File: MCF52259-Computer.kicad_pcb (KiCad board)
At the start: 6 copper layers, 110.5 x 130 mm, 4 parts, among them Y1 8MHz

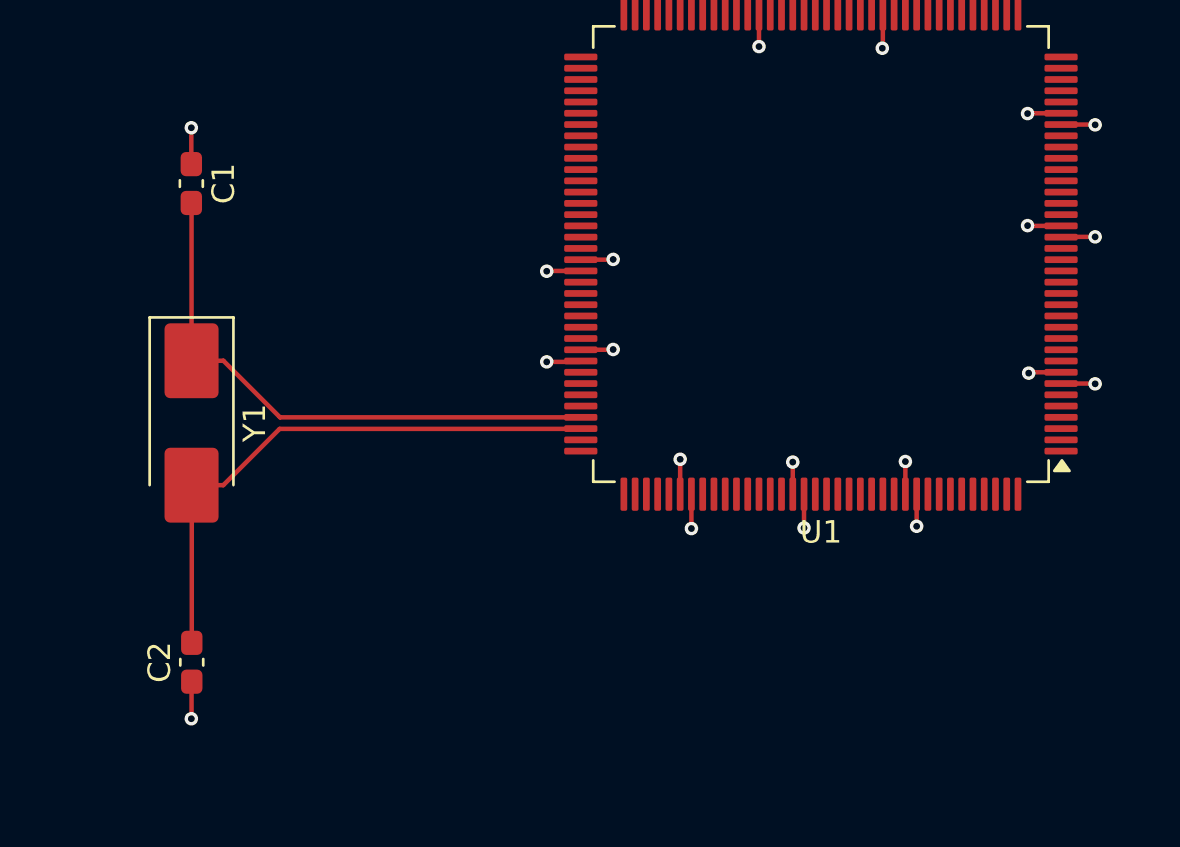
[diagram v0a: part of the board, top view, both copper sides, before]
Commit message: Configured Clock Modes Correctly
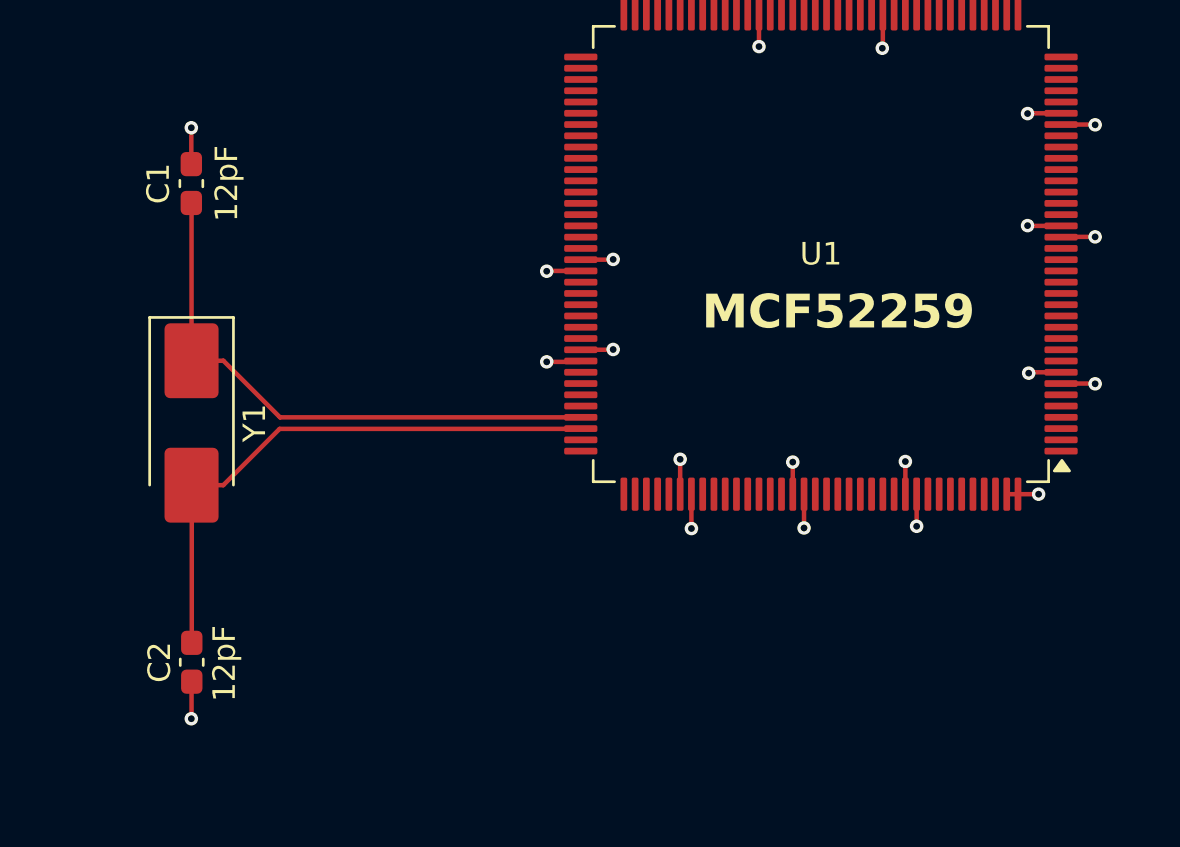
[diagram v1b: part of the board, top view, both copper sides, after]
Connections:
- C1 pad 1: GND -> VSS
- C2 pad 1: GND -> VSS
- U1 pad 113: FEC_TXD2 -> FEC_TXD0
- U1 pad 133: FB_A17 -> FB_A16
- U1 pad 143: CLKMOD0 -> VDD
- U1 pad 144: CLKMOD1 -> VDD
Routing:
- net GND: track 3.24 -> 0.00 mm, vias 2 -> 0
- net VSS: track 14.7 -> 18.0 mm, vias 10 -> 12
- net VDD: track 15.3 -> 16.7 mm, vias 10 -> 11
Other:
- board text added: "MCF52259"

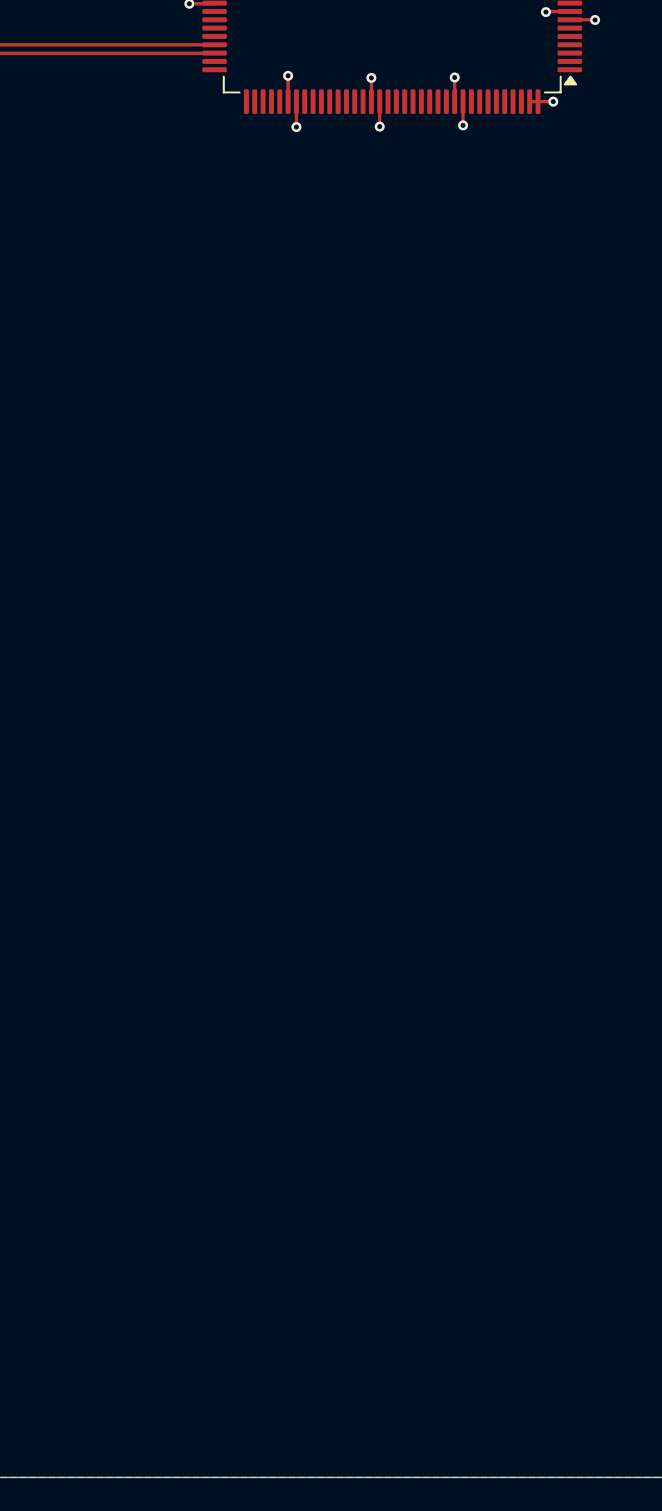
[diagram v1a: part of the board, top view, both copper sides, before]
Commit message: Added Reset Circuitry
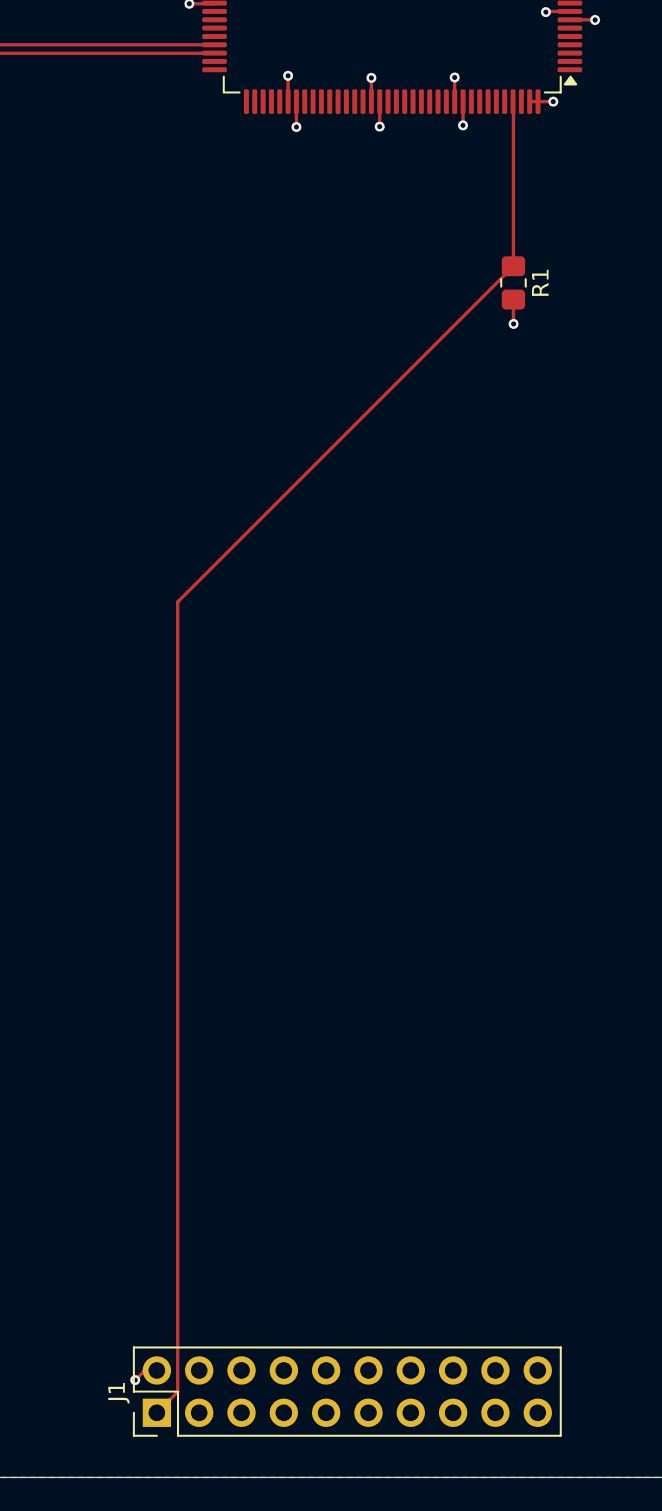
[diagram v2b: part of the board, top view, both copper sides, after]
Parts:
- added J1: Conn_02x10_Counter_Clockwise, Connector_PinHeader_2.54mm:PinHeader_2x10_P2.54mm_Vertical, F.Cu at (89.5, 157.6)
- added R1: 330Ω, Resistor_SMD:R_0805_2012Metric_Pad1.20x1.40mm_HandSolder, F.Cu at (110.8, 89.8)
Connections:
- U1 pad 142: /RSTOUT -> unconnected-(U1-/RSTOUT-Pad142)
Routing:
- net /RSTIN: track 0.00 -> 87.6 mm
- net VSS: track 18.0 -> 19.5 mm, vias 12 -> 13
- net VDD: track 16.7 -> 18.2 mm, vias 11 -> 12

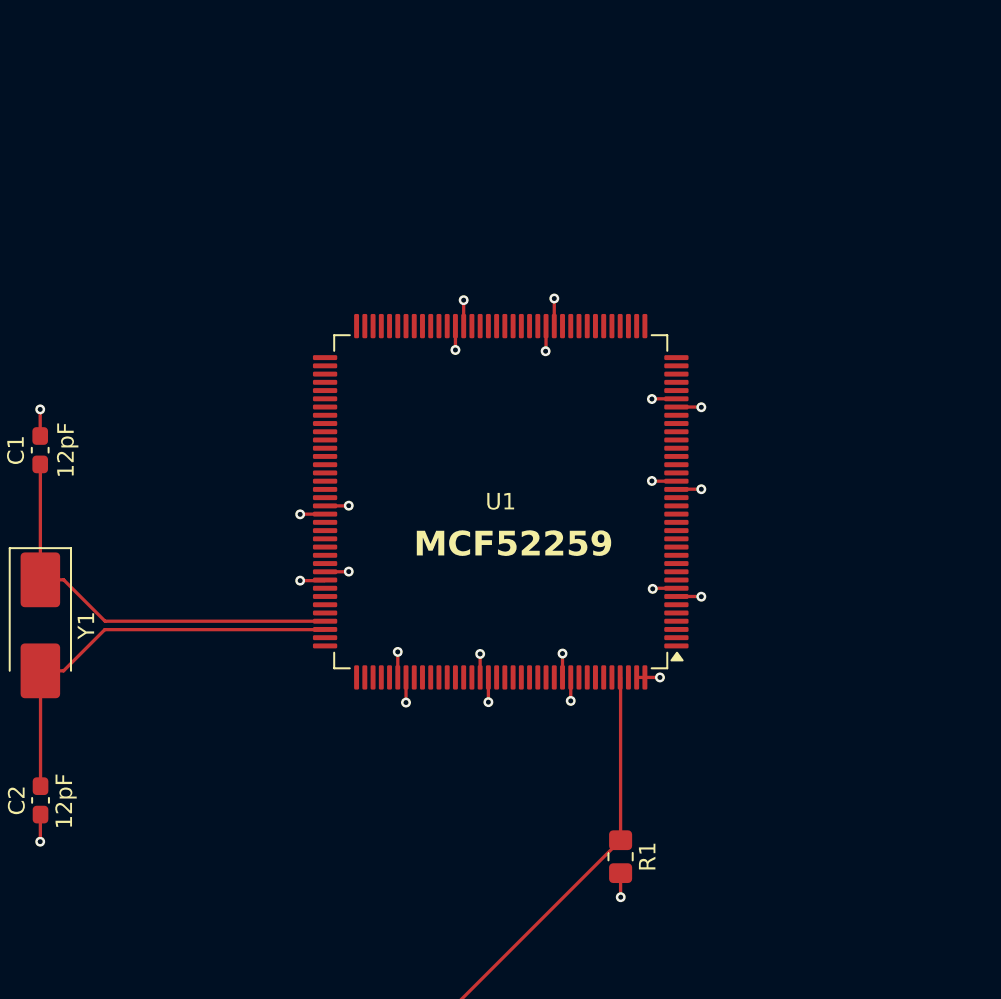
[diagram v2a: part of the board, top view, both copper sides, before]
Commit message: Added Decoupling Caps
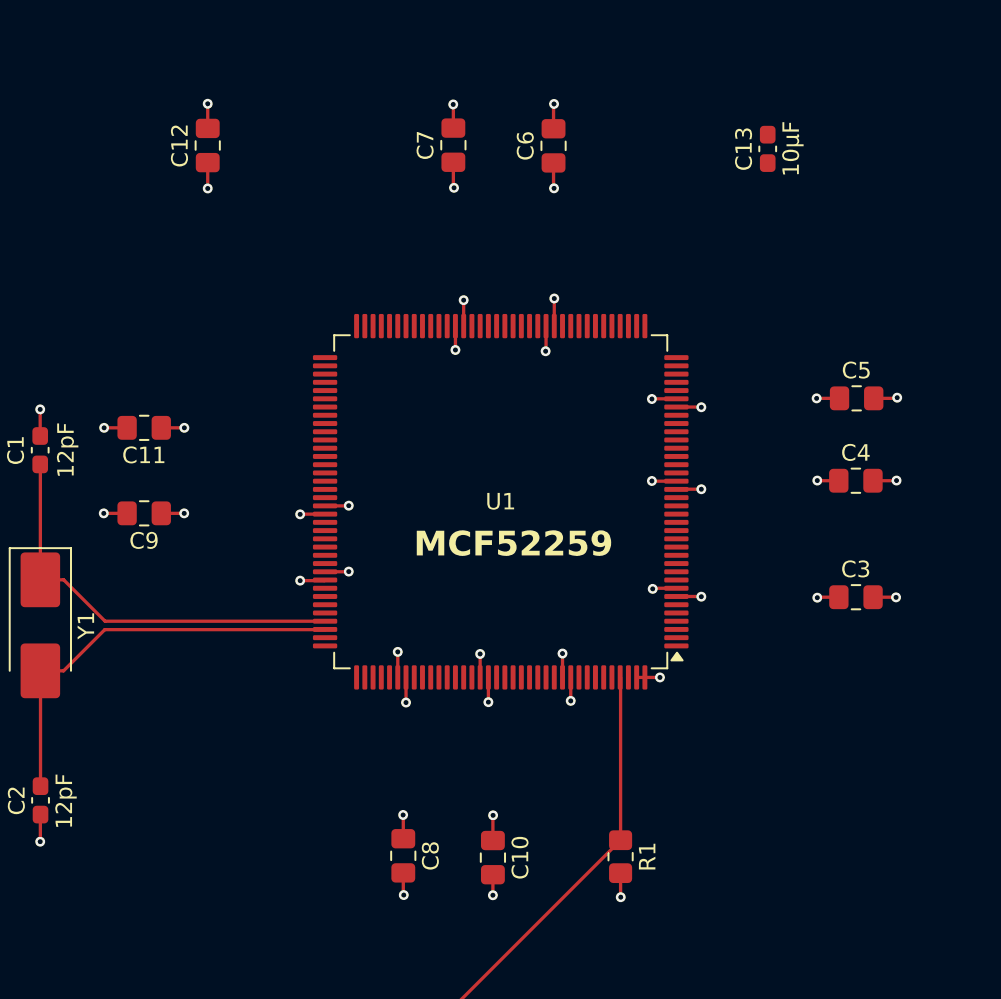
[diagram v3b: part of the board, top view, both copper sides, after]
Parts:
- added C10: 0.1µF, Capacitor_SMD:C_0805_2012Metric_Pad1.18x1.45mm_HandSolder, F.Cu at (103.1, 89.9)
- added C11: 0.1µF, Capacitor_SMD:C_0805_2012Metric_Pad1.18x1.45mm_HandSolder, F.Cu at (81.9, 63.8)
- added C12: 0.1µF, Capacitor_SMD:C_0805_2012Metric_Pad1.18x1.45mm_HandSolder, F.Cu at (85.8, 46.6)
- added C13: 10µF, Capacitor_SMD:C_0603_1608Metric_Pad1.08x0.95mm_HandSolder, F.Cu at (119.8, 46.8)
- added C3: 0.1µF, Capacitor_SMD:C_0805_2012Metric_Pad1.18x1.45mm_HandSolder, F.Cu at (125.1, 74.1)
- added C4: 0.1µF, Capacitor_SMD:C_0805_2012Metric_Pad1.18x1.45mm_HandSolder, F.Cu at (125.1, 67.0)
- added C5: 0.1µF, Capacitor_SMD:C_0805_2012Metric_Pad1.18x1.45mm_HandSolder, F.Cu at (125.2, 62.0)
- added C6: 0.1µF, Capacitor_SMD:C_0805_2012Metric_Pad1.18x1.45mm_HandSolder, F.Cu at (106.8, 46.7)
- added C7: 0.1µF, Capacitor_SMD:C_0805_2012Metric_Pad1.18x1.45mm_HandSolder, F.Cu at (100.7, 46.6)
- added C8: 0.1µF, Capacitor_SMD:C_0805_2012Metric_Pad1.18x1.45mm_HandSolder, F.Cu at (97.7, 89.8)
- added C9: 0.1µF, Capacitor_SMD:C_0805_2012Metric_Pad1.18x1.45mm_HandSolder, F.Cu at (81.9, 69.0)
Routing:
- net VDD: track 18.2 -> 32.7 mm, vias 12 -> 22
- net VSS: track 19.5 -> 33.7 mm, vias 13 -> 23

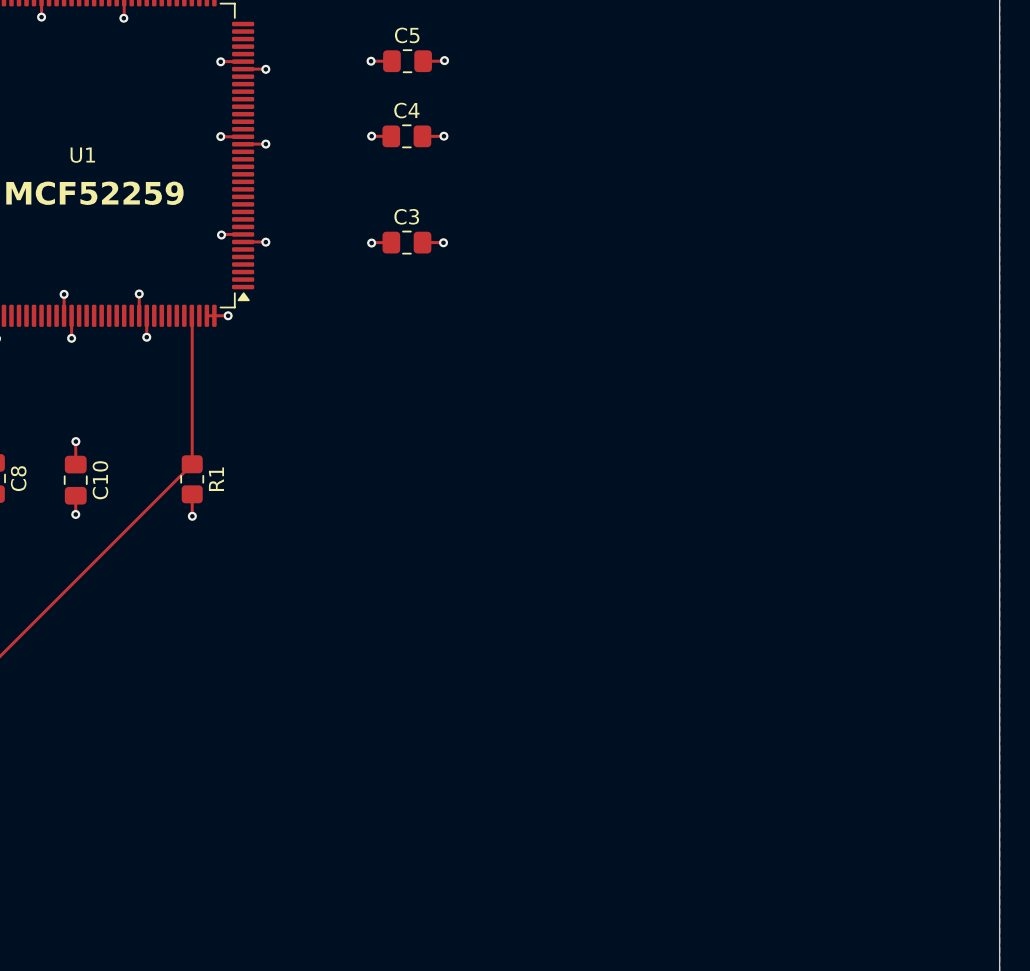
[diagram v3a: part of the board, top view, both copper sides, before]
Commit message: Added SD-Card
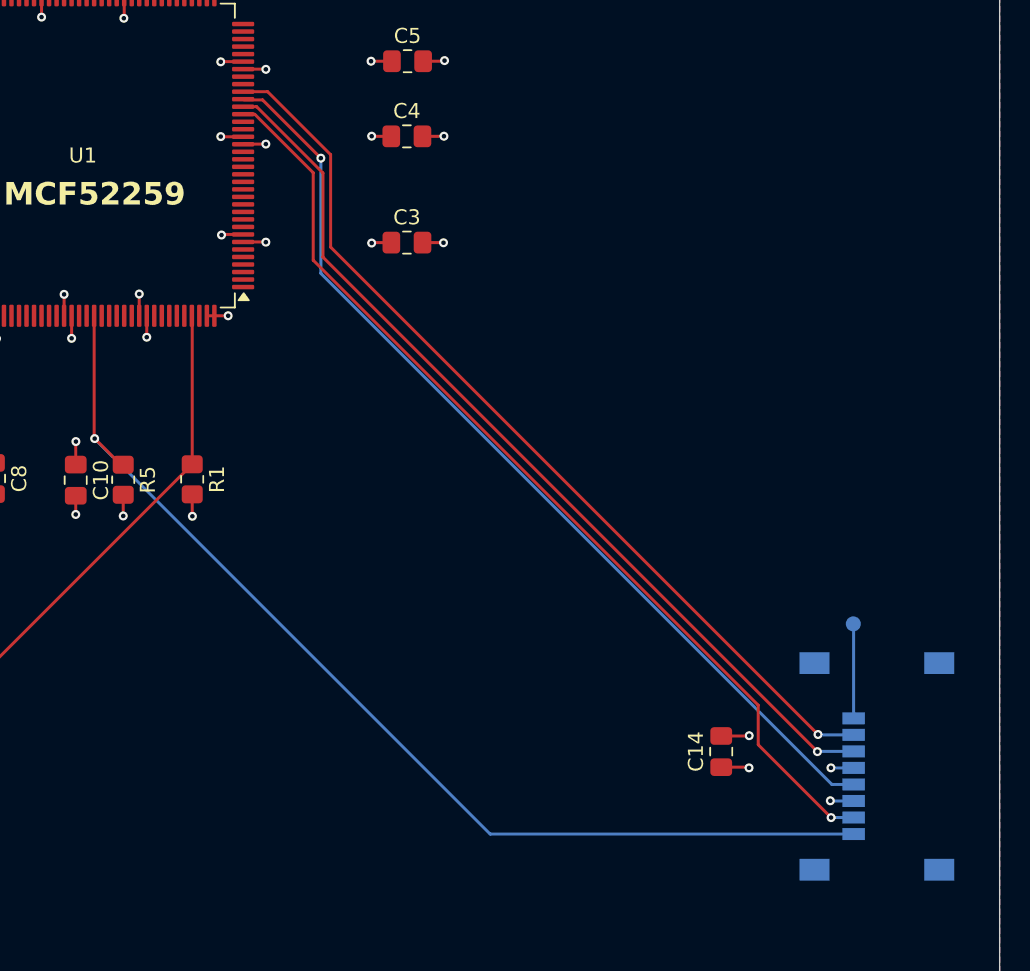
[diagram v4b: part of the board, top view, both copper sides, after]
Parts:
- added C14: 0.1µF, Capacitor_SMD:C_0805_2012Metric_Pad1.18x1.45mm_HandSolder, F.Cu at (146.1, 107.9)
- added J2: Micro_SD_Card, Connector_Card:microSD_HC_Wuerth_693072010801, B.Cu at (156.4, 108.9)
- added R5: 22kΩ, Resistor_SMD:R_0805_2012Metric_Pad1.20x1.40mm_HandSolder, F.Cu at (106.3, 89.8)
- added TP1: SD0_D2, TestPoint:TestPoint_Pad_D1.0mm, B.Cu at (154.8, 99.4)
- R1: value 330Ω -> 22kΩ
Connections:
- U1 pad 24: QSDI -> QSPI_MISO
- U1 pad 25: QSD0 -> QSPI_MOSI
- U1 pad 26: SCK -> QSPI_CLK
- U1 pad 27: PCS0 -> QSPI_CS0
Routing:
- net /IRQ5: track 0.00 -> 72.2 mm, vias 0 -> 1
- net QSPI_MISO: track 0.00 -> 65.0 mm, vias 0 -> 1
- net QSPI_CLK: track 0.00 -> 63.9 mm, vias 0 -> 1
- net QSPI_CS0: track 0.00 -> 62.0 mm, vias 0 -> 1
- net QSPI_MOSI: track 0.00 -> 61.7 mm, vias 0 -> 1
- net Net-(J2-DAT2): track 0.00 -> 6.29 mm
- net VDD: track 32.7 -> 37.5 mm, vias 22 -> 25
- net VSS: track 33.7 -> 37.1 mm, vias 23 -> 25
